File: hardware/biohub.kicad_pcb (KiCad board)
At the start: 4 copper layers, 89 x 55 mm, 130 parts, among them J1 CONNECTOR, J2 Conn_02x13_Odd_Even, U1 ADUM1412BRWZ, U10 AD8244BRMZ, U11 AD8244BRMZ, U12 TPD4E1B06DCKR, U13 TPD4E1B06DCKR, U14 MCP1603T-330I, U15 USBLC6-2SC6, U2 MCP2210-I_SS, U3 ADUM6020, U4 ADM8660ARZ, U5 ADP7142AUJZ-2.5-R7, U6 ADP7182AUJZ-2.5-R7, U7 ADS1299IPAG, U8 AD8244BRMZ, U9 AD8244BRMZ

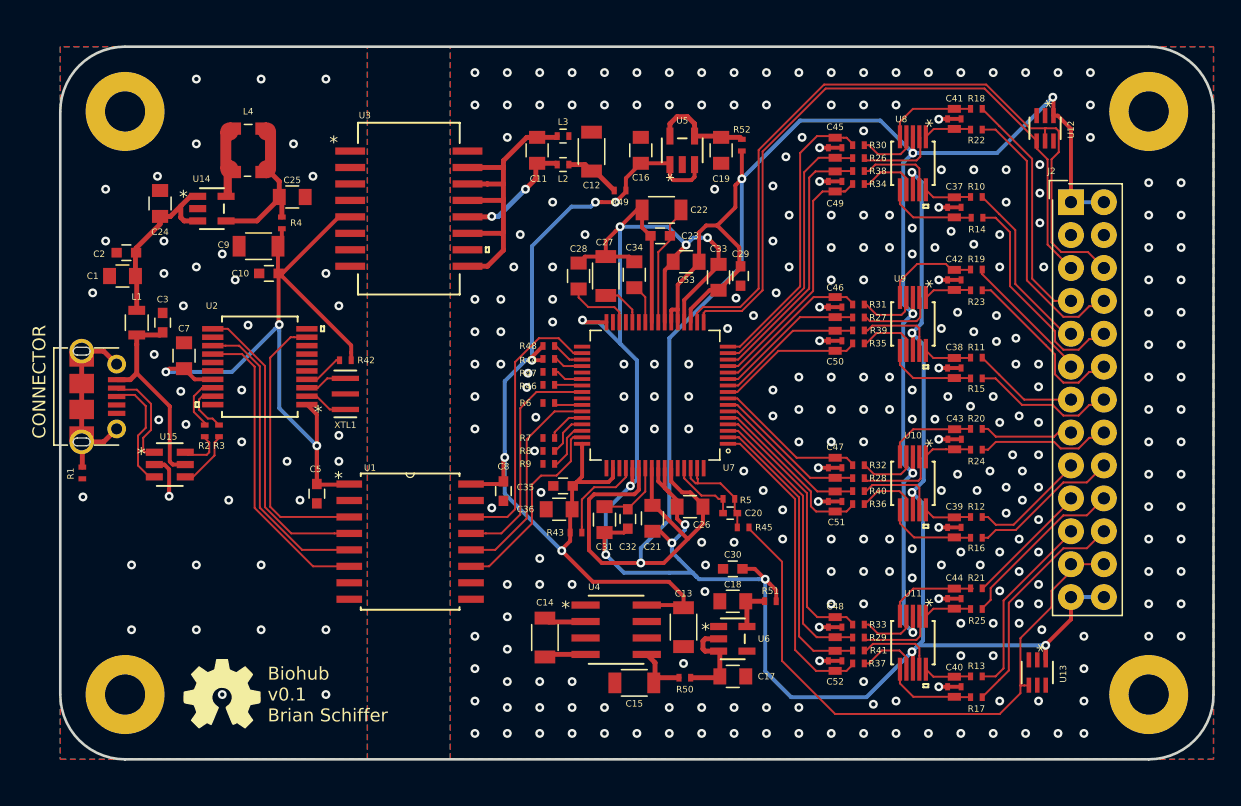
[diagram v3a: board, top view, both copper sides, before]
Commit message: Expanded outline to fix mounting hole interference
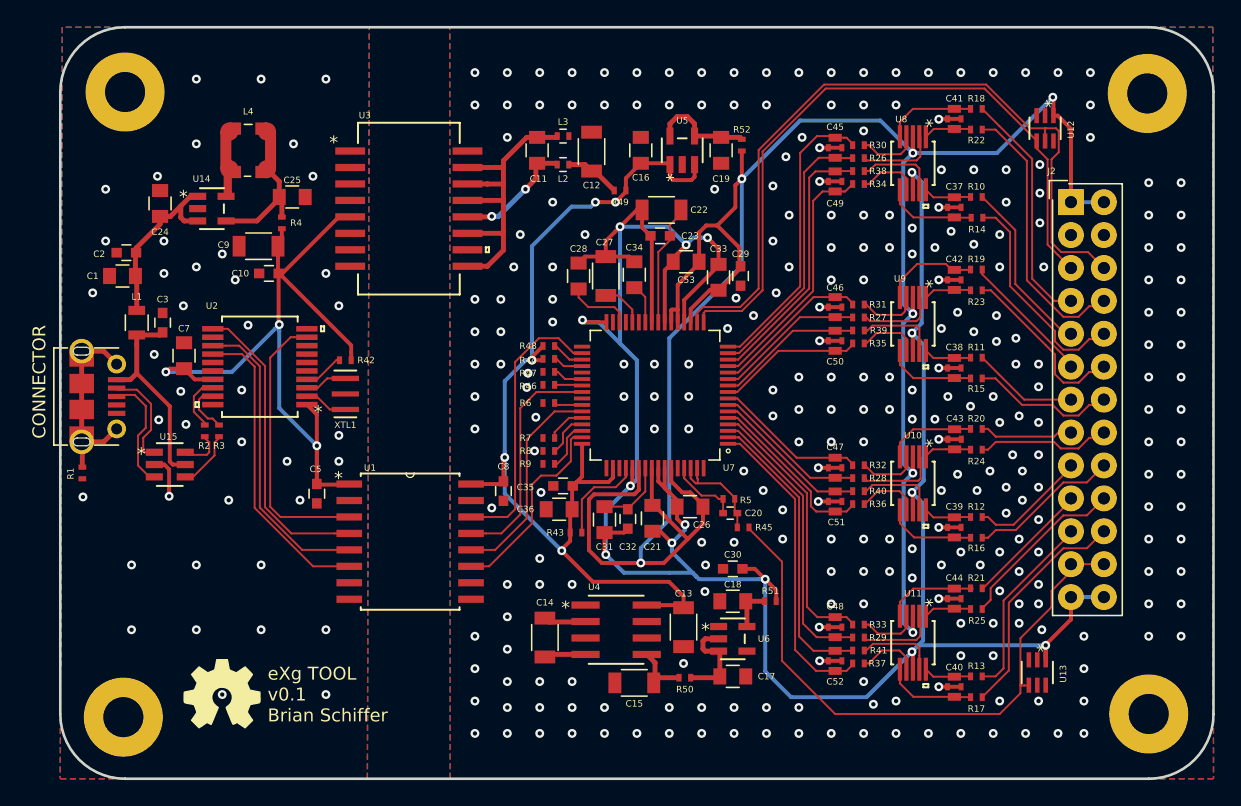
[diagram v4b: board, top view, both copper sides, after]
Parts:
- moved ? 1.75 mm to (110.0, 117.0)
- moved ? 1.50 mm to (186.1, 115.5)
- moved ? 1.50 mm to (111.2, 70.7)
- moved ? 1.39 mm to (187.5, 69.5)
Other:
- board size 89 x 55 mm -> 89 x 58 mm
- board text added: "eXg TOOL v0.1 Brian Schiffer"
- board text removed: "Biohub v0.1 Brian Schiffer"
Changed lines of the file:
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@@
     (40 Dwgs.User user hide)
     (41 Cmts.User user hide)
-    (42 Eco1.User user hide)
+    (42 Eco1.User user)
     (43 Eco2.User user)
     (44 Edge.Cuts user)
@@
   )
   (module OpenCamera:MOUNTING_HOLE locked (layer F.Cu)
-    (at 186.087 113.984)
+    (at 186.087 115.484)
     (fp_text reference "" (at 0 5.2) (layer Eco2.User) hide
       (effects (font (size 0.5 0.5) (thickness 0.125)))
@@
   )
   (module OpenCamera:MOUNTING_HOLE locked (layer F.Cu)
-    (at 110.135 115.254)
+    (at 110 117)
     (fp_text reference "" (at 0 5.2) (layer Eco2.User) hide
       (effects (font (size 0.5 0.5) (thickness 0.125)))
@@
   )
   (module OpenCamera:MOUNTING_HOLE locked (layer F.Cu)
-    (at 111.151 72.159)
+    (at 111.151 70.659)
     (fp_text reference "" (at 0 5.2) (layer Eco2.User) hide
       (effects (font (size 0.5 0.5) (thickness 0.125)))
@@
   )
   (module OpenCamera:MOUNTING_HOLE locked (layer F.Cu)
-    (at 187.611 70.889)
+    (at 187.5 69.5)
     (fp_text reference "" (at 0 5.2) (layer Eco2.User) hide
       (effects (font (size 0.5 0.5) (thickness 0.125)))
@@
   (gr_poly (pts (xy 136 66.5) (xy 137 66.5) (xy 137 71.1) (xy 136 71.1)) (layer F.Mask) (width 0.15))
   (gr_poly (pts (xy 136.2 66.5) (xy 136.2 67.5) (xy 184.5 67.5) (xy 184.5 66.5)) (layer F.Mask) (width 0.15))
-  (gr_arc (start 109.5 115) (end 104.5 115) (angle -90) (layer Edge.Cuts) (width 0.2))
-  (gr_arc (start 109.5 70) (end 109.5 65) (angle -90) (layer Edge.Cuts) (width 0.2))
-  (gr_arc (start 188.5 70) (end 193.5 70) (angle -90) (layer Edge.Cuts) (width 0.2))
-  (gr_arc (start 188.5 115) (end 188.5 120) (angle -90) (layer Edge.Cuts) (width 0.2))
+  (gr_arc (start 109.5 116.5) (end 104.5 116.5) (angle -90) (layer Edge.Cuts) (width 0.2))
+  (gr_arc (start 109.5 68.5) (end 109.5 63.5) (angle -90) (layer Edge.Cuts) (width 0.2))
+  (gr_arc (start 188.5 68.5) (end 193.5 68.5) (angle -90) (layer Edge.Cuts) (width 0.2))
+  (gr_arc (start 188.5 116.5) (end 188.5 121.5) (angle -90) (layer Edge.Cuts) (width 0.2))
   (dimension 89 (width 0.3) (layer Eco1.User)
     (gr_text "89.000 mm" (at 148.984558 41.817599) (layer Eco1.User)
@@
     (arrow2b (pts (xy 104.484558 43.917599) (xy 105.611062 43.331178)))
   )
-  (gr_line (start 109.5 65) (end 188.5 65) (angle 90) (layer Edge.Cuts) (width 0.2032))
-  (gr_line (start 104.5 70) (end 104.5 115) (angle 90) (layer Edge.Cuts) (width 0.2032))
-  (gr_line (start 109.5 120) (end 188.5 120) (angle 90) (layer Edge.Cuts) (width 0.2))
-  (gr_line (start 193.5 115) (end 193.5 70) (angle 90) (layer Edge.Cuts) (width 0.2032))
-  (gr_text "Biohub\nv0.1\nBrian Schiffer" (at 120.5 115) (layer F.SilkS)
+  (gr_line (start 109.5 63.5) (end 188.5 63.5) (angle 90) (layer Edge.Cuts) (width 0.2032))
+  (gr_line (start 104.5 68.5) (end 104.5 116.5) (angle 90) (layer Edge.Cuts) (width 0.2032))
+  (gr_line (start 109.5 121.5) (end 188.5 121.5) (angle 90) (layer Edge.Cuts) (width 0.2))
+  (gr_line (start 193.5 116.5) (end 193.5 68.5) (angle 90) (layer Edge.Cuts) (width 0.2032))
+  (gr_text "eXg TOOL\nv0.1\nBrian Schiffer" (at 120.5 115) (layer F.SilkS)
     (effects (font (size 1 1) (thickness 0.1524)) (justify left))
   )
-  (dimension 55 (width 0.3) (layer Eco1.User)
-    (gr_text "55.000 mm" (at 206.807086 92.6 270) (layer Eco1.User)
+  (dimension 58 (width 0.3) (layer Eco1.User)
+    (gr_text "58.000 mm" (at 206.873 92.5 270) (layer Eco1.User)
       (effects (font (size 1.5 1.5) (thickness 0.3)))
     )
-    (feature1 (pts (xy 179.434086 120.1) (xy 205.293507 120.1)))
-    (feature2 (pts (xy 179.434086 65.1) (xy 205.293507 65.1)))
-    (crossbar (pts (xy 204.707086 65.1) (xy 204.707086 120.1)))
-    (arrow1a (pts (xy 204.707086 120.1) (xy 204.120665 118.973496)))
-    (arrow1b (pts (xy 204.707086 120.1) (xy 205.293507 118.973496)))
-    (arrow2a (pts (xy 204.707086 65.1) (xy 204.120665 66.226504)))
-    (arrow2b (pts (xy 204.707086 65.1) (xy 205.293507 66.226504)))
+    (feature1 (pts (xy 179.5 121.5) (xy 205.359421 121.5)))
+    (feature2 (pts (xy 179.5 63.5) (xy 205.359421 63.5)))
+    (crossbar (pts (xy 204.773 63.5) (xy 204.773 121.5)))
+    (arrow1a (pts (xy 204.773 121.5) (xy 204.186579 120.373496)))
+    (arrow1b (pts (xy 204.773 121.5) (xy 205.359421 120.373496)))
+    (arrow2a (pts (xy 204.773 63.5) (xy 204.186579 64.626504)))
+    (arrow2b (pts (xy 204.773 63.5) (xy 205.359421 64.626504)))
   )
-  (via (at 112.9 99.7) (size 0.6858) (drill 0.3302) (layers F.Cu B.Cu) (net 3))
-  (via (at 112.1 93.8) (size 0.6858) (drill 0.3302) (layers F.Cu B.Cu) (net 3))
   (segment (start 125.3 93) (end 126.5 93) (width 0.1524) (layer F.Cu) (net 2))
   (segment (start 123.5322 91.974999) (end 124.274999 91.974999) (width 0.1524) (layer F.Cu) (net 2))
   (segment (start 124.274999 91.974999) (end 125.3 93) (width 0.1524) (layer F.Cu) (net 2))
+  (via (at 112.9 99.7) (size 0.6858) (drill 0.3302) (layers F.Cu B.Cu) (net 3))
+  (via (at 112.1 93.8) (size 0.6858) (drill 0.3302) (layers F.Cu B.Cu) (net 3))
   (via (at 112 75) (size 0.6858) (drill 0.3302) (layers F.Cu B.Cu) (net 3))
   (via (at 125 115) (size 0.6858) (drill 0.3302) (layers F.Cu B.Cu) (net 3))
@@
     (polygon
       (pts
-        (xy 128.2 120) (xy 128.2 65) (xy 104.5 65) (xy 104.5 120)
+        (xy 128.2 121.5) (xy 128.35 63.5) (xy 104.65 63.5) (xy 104.5 121.5)
       )
     )
@@
     (polygon
       (pts
-        (xy 134.6 120) (xy 134.6 65) (xy 193.5 65) (xy 193.5 120)
+        (xy 134.6 121.5) (xy 134.55 63.5) (xy 193.45 63.5) (xy 193.5 121.5)
       )
     )
@@
     (polygon
       (pts
-        (xy 134.6 120) (xy 134.6 65) (xy 193.5 65) (xy 193.5 120)
+        (xy 134.6 121.5) (xy 134.55 63.5) (xy 193.45 63.5) (xy 193.5 121.5)
       )
     )
@@
     (polygon
       (pts
-        (xy 134.6 120) (xy 134.6 65) (xy 193.5 65) (xy 193.5 120)
+        (xy 134.6 121.5) (xy 134.55 63.5) (xy 193.45 63.5) (xy 193.5 121.5)
       )
     )
@@
     (polygon
       (pts
-        (xy 128.2 120) (xy 104.5 120) (xy 104.5 65) (xy 128.2 65)
+        (xy 128.35 121.5) (xy 104.65 121.5) (xy 104.5 63.5) (xy 128.2 63.5)
       )
     )
@@
     (polygon
       (pts
-        (xy 128.2 120) (xy 128.2 65) (xy 104.5 65) (xy 104.5 120)
+        (xy 128.2 121.5) (xy 128.35 63.5) (xy 104.65 63.5) (xy 104.5 121.5)
       )
     )
@@
     (polygon
       (pts
-        (xy 128.2 120) (xy 128.2 65) (xy 104.5 65) (xy 104.5 120)
+        (xy 128.2 121.5) (xy 128.35 63.5) (xy 104.65 63.5) (xy 104.5 121.5)
       )
     )
@@
     (polygon
       (pts
-        (xy 134.6 120) (xy 134.6 65) (xy 193.5 65) (xy 193.5 120)
+        (xy 134.6 121.5) (xy 134.55 63.5) (xy 193.45 63.5) (xy 193.5 121.5)
       )
     )

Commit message: Updated solder mask & paste clearance
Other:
- rule pad_to_mask_clearance: 0.051 -> 0.0508
- rule solder_mask_min_width: 0.25 -> 0.1016
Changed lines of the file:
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@@
     (pad_size 1.524 1.524)
     (pad_drill 0.762)
-    (pad_to_mask_clearance 0.051)
-    (solder_mask_min_width 0.25)
+    (pad_to_mask_clearance 0.0508)
+    (solder_mask_min_width 0.1016)
+    (pad_to_paste_clearance -0.0254)
     (aux_axis_origin 0 0)
     (visible_elements 7FFFFFFF)
